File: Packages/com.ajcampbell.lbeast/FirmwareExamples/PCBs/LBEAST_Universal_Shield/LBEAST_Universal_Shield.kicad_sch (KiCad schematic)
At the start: 46 parts, among them J1 Barrel_Jack_Switch, J1 MTJ-883X1, J10 JST-XH 2-Pin Fan, J2 MTJ-883X1, J3 MTJ-883X1, J4 MTJ-883X1, J5 MTJ-883X1, J6 MTJ-883X1, J7 MTJ-883X1, J8 MTJ-883X1, J9 CAN BUS, Q1 IRLZ44N, U1 LM2576HVS-5, U5 LAN8720A, U8 ADM3057ExRW, Y1 25MHz

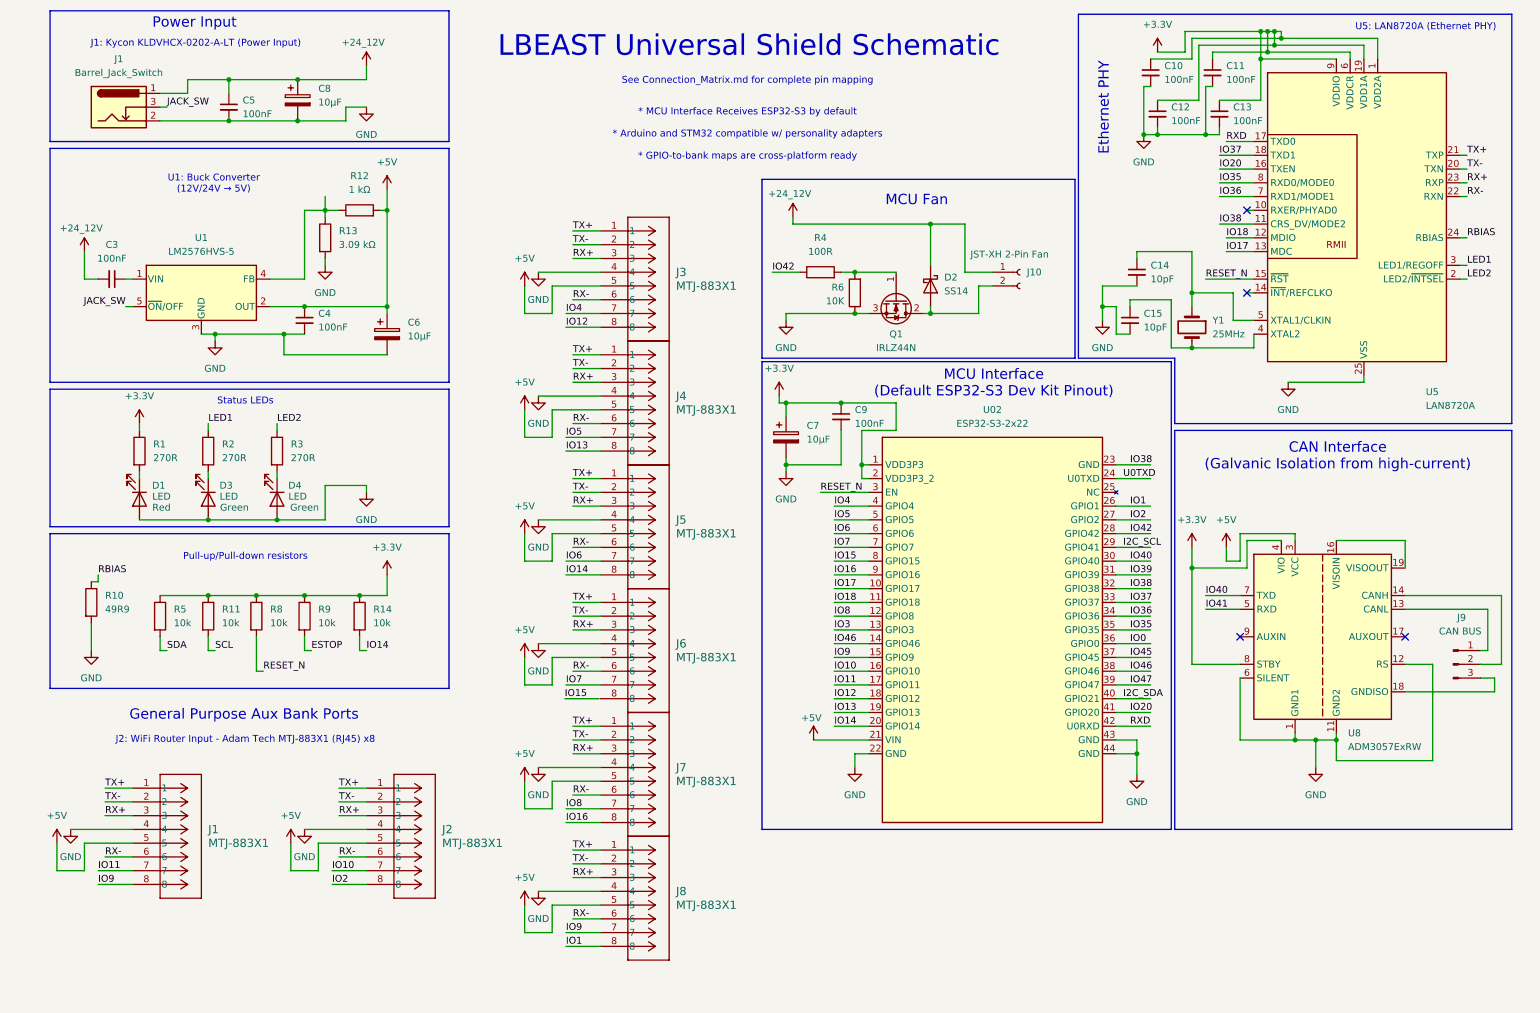
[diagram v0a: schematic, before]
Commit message: complete alpha universal shield pcb
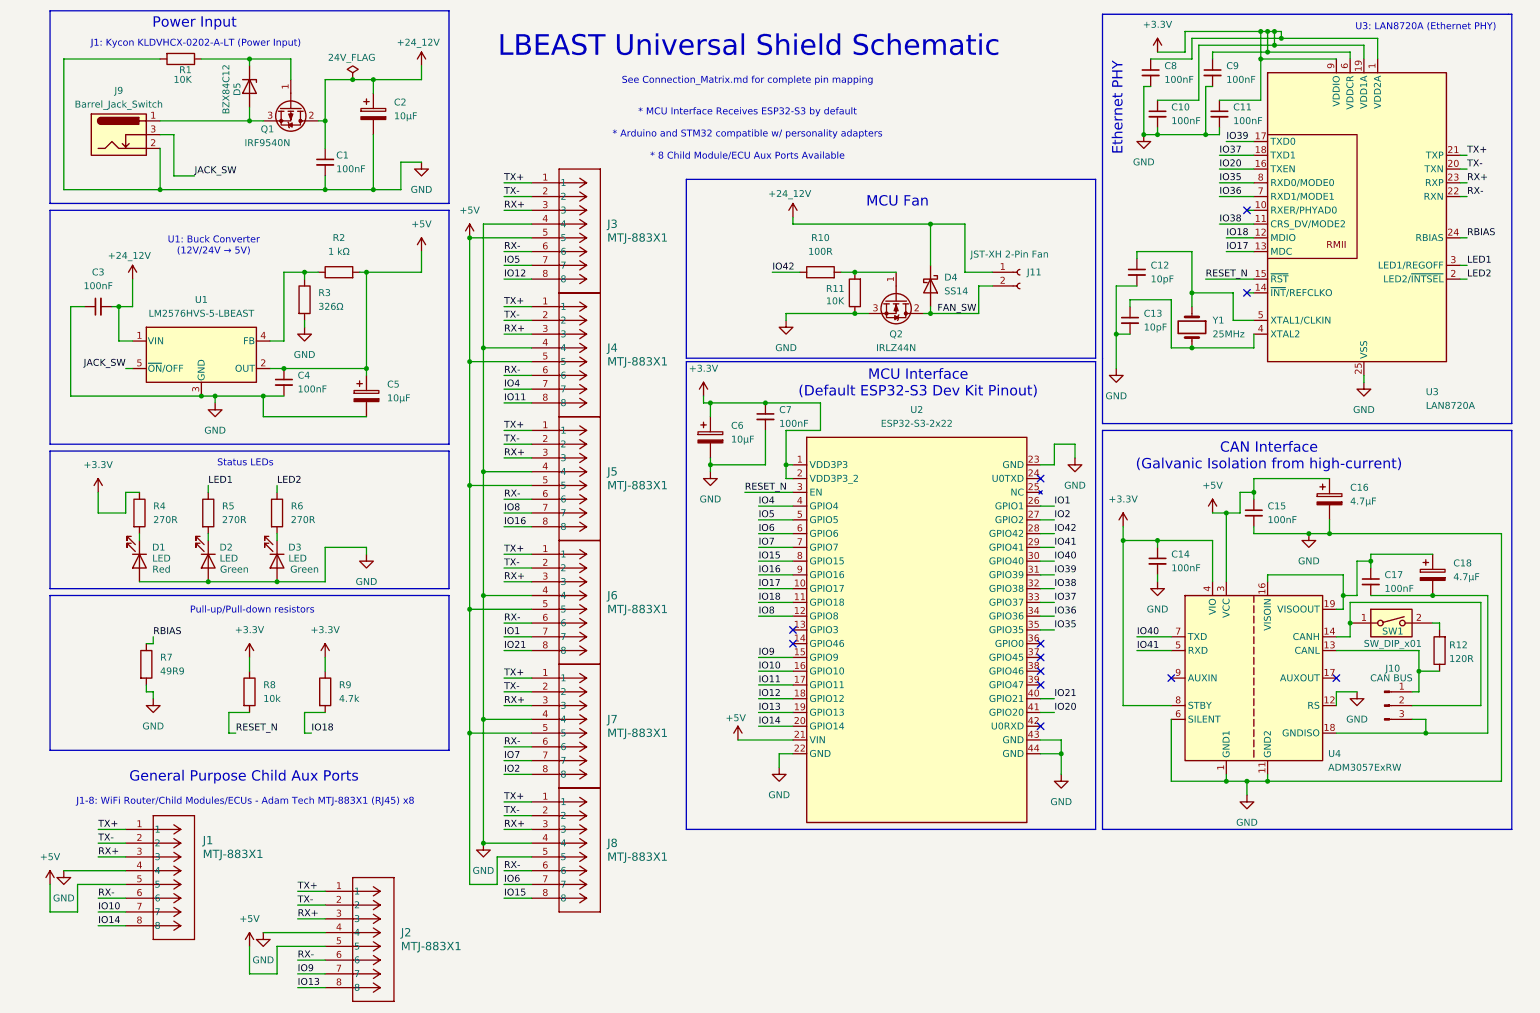
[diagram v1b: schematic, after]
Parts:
- removed R11, R14, R5: 10k, Resistor_SMD:R_0805_2012Metric, symbol Device:R
- removed U1: LM2576HVS-5, Package_TO_SOT_SMD:TO-263-5_TabPin3, symbol Regulator_Switching:LM2576HVS-5
- added C14, C15, C17: 100nF, Capacitor_SMD:C_0805_2012Metric, symbol Device:C_Small
- added C16, C18: 4.7µF, Capacitor_Tantalum_SMD:CP_EIA-3216-18_Kemet-A, symbol Device:C_Polarized
- added D5: BZX84C12, Package_TO_SOT_SMD:SOT-23, symbol Diode:BZX84Cxx
- added Q1: IRF9540N, Package_TO_SOT_THT:TO-220-3_Vertical, symbol Transistor_FET:IRF9540N
- added R1: 10K, Resistor_SMD:R_0805_2012Metric, symbol Device:R
- added R12: 120R, Resistor_SMD:R_0805_2012Metric, symbol Device:R
- added SW1: SW_DIP_x01, Button_Switch_SMD:SW_DIP_SPSTx01_Slide_6.7x4.1mm_W6.73mm_P2.54mm_LowProfile_JPin, symbol Switch:SW_DIP_x01
- added U1: LM2576HVS-5-LBEAST, Package_TO_SOT_SMD:TO-263-5_TabPin3, symbol LBEAST_Symbols:LM2576HVS-5-LBEAST
- added U2: ESP32-S3-2x22, LBEASTLibrary:ESP32-S3_2x22_Header_v3, symbol ESP32-S3-2x22:ESP32-S3-2x22
- J1, J2, J3, J4, J5, J6, J7, J8: footprint CONN_MTJ-883X1_ADM -> LBEASTLibrary:CONN_MTJ-883X1_ADM
- J10: renamed from J9; footprint (none) -> LBEASTLibrary:JST_XH_B3B-XH-A_1x03_P2.50mm_Vertical
- J9: renamed from J1; footprint (none) -> Connector_BarrelJack:BarrelJack_Kycon_KLDX-0202-xC_Horizontal
- R3: renamed from R13; value 3.09 kΩ -> 326Ω
- R9: value 10k -> 4.7k
- renumbered C5 to C1, C12 to C10, C13 to C11, C14 to C12, C15 to C13, C8 to C2, C6 to C5, C7 to C6, C9 to C7, C10 to C8, C11 to C9, D3 to D2, D4 to D3, D2 to D4, J10 to J11, Q1 to Q2, R4 to R10, R6 to R11, R12 to R2, R1 to R4, R2 to R5, R3 to R6, R10 to R7, U5 to U3, U8 to U4
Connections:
- net ESTOP is gone; now on net IO18: R9.2
- net RXD is gone; now on net IO39: U3.17 (TXD0)
- net +24_12V: now also Q1.2 (D), U1.1 (VIN); no longer J9.1
- net +3.3V: now also C14.1, U2.1 (VDD3P3), U2.2 (VDD3P3_2); no longer C1.2, C10.2, C11.2, C12.2, C13.2, C2.2, C4.1, C4.2, C5.1, C5.2, C6.2, C7.2, C8.2, C9.2, D1.2 (A), D2.2 (A), D3.2 (A), J1.4, J1.5, J2.4, J2.5, J3.4, J3.5, J4.4, J4.5, J5.4, J5.5, J6.4, J6.5, J7.4, J7.5, J8.4, J8.5, J9.2, Q2.3 (S), R11.1, R2.2, R3.2, R7.2, U3.11 (CRS_DV/MODE2), U3.25 (VSS), U4.1 (GND1), U4.10 (GND1), U4.11 (GND2), U4.12 (RS), U4.15 (GND2), U4.2 (GND1), U4.3 (VCC), U4.6 (SILENT)
- net IO1: now also J6.7, U2.26 (GPIO1); no longer J8.8
- net IO10: now also J1.7, U2.16 (GPIO10); no longer J2.7
- net IO11: now also J4.8, U2.17 (GPIO11); no longer J1.7
- net IO12: now also U2.18 (GPIO12)
- net IO13: now also J2.8, U2.19 (GPIO13); no longer J4.8
- net IO14: now also J1.8, U2.20 (GPIO14); no longer J5.8
- net IO15: now also J8.8, U2.8 (GPIO15)
- net IO16: now also J5.8, U2.9 (GPIO16); no longer J7.8
- net IO17: now also U2.10 (GPIO17)
- net IO18: now also U2.11 (GPIO18)
- net IO2: now also J7.8, U2.27 (GPIO2); no longer J2.8
- net IO20: now also U2.41 (GPIO20)
- net IO35: now also U2.35 (GPIO35)
- net IO36: now also U2.34 (GPIO36)
- net IO37: now also U2.33 (GPIO37)
- net IO39: now also U2.31 (GPIO39)
- net IO4: now also J4.7, U2.4 (GPIO4); no longer J3.7
- net IO40: now also U2.30 (GPIO40)
- net IO41: now also U2.29 (GPIO41)
- net IO42: now also U2.28 (GPIO42)
- net IO5: now also J3.7, U2.5 (GPIO5); no longer J4.7
- net IO6: now also J8.7, U2.6 (GPIO6); no longer J5.7
- net IO7: now also J7.7, U2.7 (GPIO7); no longer J6.7
- net IO8: now also J5.7, U2.12 (GPIO8); no longer J7.7
- net IO9: now also J2.7, U2.15 (GPIO9); no longer J1.8, J8.7
- net JACK_SW: now also U1.5 (~{ON}/OFF)
- net RESET_N: now also U2.3 (EN)
- net FAN_SW: now reaches D4.2 (A), J11.2 (Pin_2), Q2.2 (D)
- net GND: now reaches C3.1
- net GND: now also C1.2, C10.2, C11.2, C12.2, C13.2, C2.2, C4.2, C5.2, C6.2, C7.2, C8.2, C9.2, D1.2 (A), D2.2 (A), D3.2 (A), J1.4, J2.4, J3.4, J4.4, J5.4, J6.4, J7.4, J8.4, J9.2, Q2.3 (S), R11.1, R3.2, R7.2, U3.25 (VSS), U4.1 (GND1), U4.10 (GND1), U4.11 (GND2), U4.12 (RS), U4.15 (GND2), U4.2 (GND1), U4.6 (SILENT), C14.2, C15.2, C16.2, R1.2, U1.3 (GND), U2.22 (GND), U2.23 (GND), U2.43 (GND), U2.44 (GND)
- net at J10.1 (Pin_1), U4.13 (CANL): now also R12.1
- net at J10.2 (Pin_2), U4.14 (CANH): now also SW1.1
- net at U4.16 (VISOIN), U4.19 (VISOOUT): now also C17.1, C18.1
- net at J10.3 (Pin_3), U4.18 (GNDISO), U4.20 (GNDISO): now also C17.2, C18.2
- net IO21: now reaches J6.8
- net IO21: now also U2.40 (GPIO21)
- net at R2.1, R3.1: now also U1.4 (FB)
- new net: D5.3 (K), Q1.1 (G), R1.1
- new net: D5.1 (A), J9.1, Q1.3 (S)
- new net: R12.2, SW1.2
- new net +5V: C15.1, C16.1, C4.1, C5.1, J1.5, J2.5, J3.5, J4.5, J5.5, J6.5, J7.5, J8.5, R2.2, U1.2 (OUT), U2.21 (VIN), U4.3 (VCC)
- new net IO38: U2.32 (GPIO38), U3.11 (CRS_DV/MODE2)
- no-connect marks 4 -> 12
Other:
- note added: "* MCU Interface Receives ESP32-S3 by default * Arduino and STM32 compatible w/ personality adapters * 8 Child Module/ECU Aux Ports Available"
- note added: "General Purpose Child Aux Ports"
- note added: "J1-8: WiFi Router/Child Modules/ECUs - Adam Tech MTJ-883X1 (RJ45) x8"
- note added: "U3: LAN8720A (Ethernet PHY)"
- note removed: "* MCU Interface Receives ESP32-S3 by default * Arduino and STM32 compatible w/ personality adapters * GPIO-to-bank maps are cross-platform ready"
- note removed: "General Purpose Aux Bank Ports"
- note removed: "J2: WiFi Router Input - Adam Tech MTJ-883X1 (RJ45) x8"
- note removed: "U5: LAN8720A (Ethernet PHY)"
- moved on the sheet: C1, C2, C3, C4, C5, C6, C7, D1, D2, D3, J1, J10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
